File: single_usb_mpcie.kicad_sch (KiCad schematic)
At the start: 15 parts, among them J1 91304-56-052R2, J2 USB_B_Micro, U1 AZ1117H-3.3

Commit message: Change mounting holes to #6-32
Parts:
- H1, H2, H3, H4: footprint MountingHole:MountingHole_3.2mm_M3_Pad -> parts:MountingHole_6-32_Pad
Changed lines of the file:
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@@
       (effects (font (size 1.27 1.27)) (justify left))
     )
-    (property "Footprint" "MountingHole:MountingHole_3.2mm_M3_Pad" (at 124.46 147.32 0)
+    (property "Footprint" "parts:MountingHole_6-32_Pad" (at 124.46 147.32 0)
       (effects (font (size 1.27 1.27)) hide)
     )
@@
       (effects (font (size 1.27 1.27)) (justify left))
     )
-    (property "Footprint" "MountingHole:MountingHole_3.2mm_M3_Pad" (at 124.46 142.24 0)
+    (property "Footprint" "parts:MountingHole_6-32_Pad" (at 124.46 142.24 0)
       (effects (font (size 1.27 1.27)) hide)
     )
@@
       (effects (font (size 1.27 1.27)) (justify left))
     )
-    (property "Footprint" "MountingHole:MountingHole_3.2mm_M3_Pad" (at 124.46 132.08 0)
+    (property "Footprint" "parts:MountingHole_6-32_Pad" (at 124.46 132.08 0)
       (effects (font (size 1.27 1.27)) hide)
     )
@@
       (effects (font (size 1.27 1.27)) (justify left))
     )
-    (property "Footprint" "MountingHole:MountingHole_3.2mm_M3_Pad" (at 124.46 137.16 0)
-      (effects (font (size 1.27 1.27)) hide)
-    )
+    (property "Footprint" "parts:MountingHole_6-32_Pad" (at 124.46 137.16 0)
+      (effects (font (size 1.27 1.27)) hide)
+    )

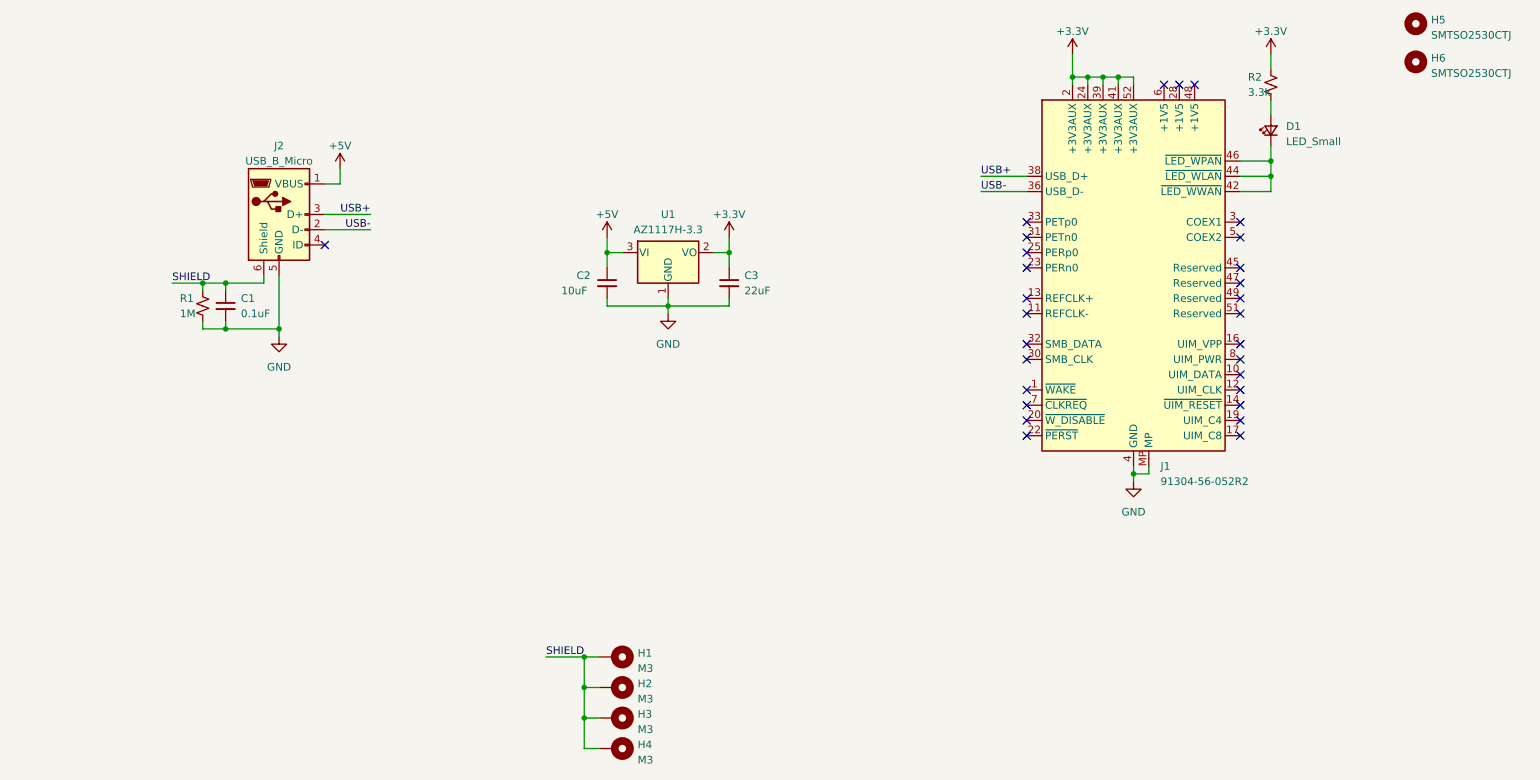
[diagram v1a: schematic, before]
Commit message: Add ESD on USB lines. Add noise filtering to VBUS. Change to a 4-layer board with ground / power planes.
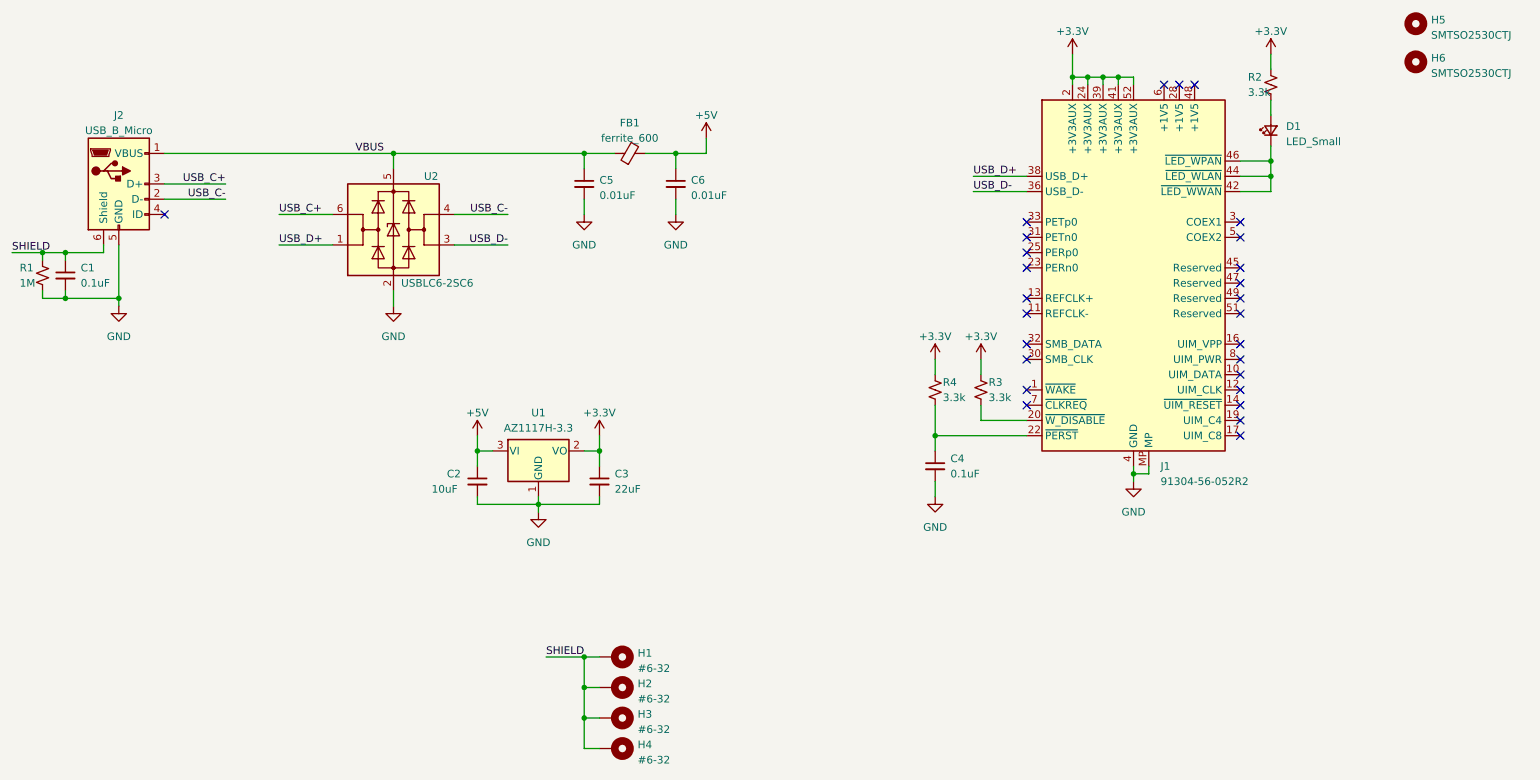
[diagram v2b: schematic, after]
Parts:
- added C4: 0.1uF, Capacitor_SMD:C_0603_1608Metric, symbol Device:C_Small
- added C5, C6: 0.01uF, Capacitor_SMD:C_0603_1608Metric, symbol Device:C_Small
- added FB1: ferrite_600, Inductor_SMD:L_0603_1608Metric, symbol Device:FerriteBead_Small
- added R3, R4: 3.3k, Resistor_SMD:R_0603_1608Metric, symbol Device:R_Small_US
- added U2: USBLC6-2SC6, Package_TO_SOT_SMD:SOT-23-6, symbol Power_Protection:USBLC6-2SC6
- C1: LCSC (none) -> C14663
- H1, H2, H3, H4: value M3 -> #6-32
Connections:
- net +3.3V: now also R3.1, R4.1
- net +5V: now also C6.1, FB1.2; no longer J2.1 (VBUS)
- net GND: now also C4.2, C5.2, C6.2, U2.2 (GND)
- net at J1.20 (~{W_DISABLE}): now also R3.2
- net at J1.22 (~{PERST}): now also C4.1, R4.2
- net USB+ renamed USB_C+
- net USB_C+: now also U2.6 (I/O1); no longer J1.38 (USB_D+)
- net USB- renamed USB_C-
- net USB_C-: now also U2.4 (I/O2); no longer J1.36 (USB_D-)
- new net USB_D+: J1.38 (USB_D+), U2.1 (I/O1)
- new net USB_D-: J1.36 (USB_D-), U2.3 (I/O2)
- new net VBUS: C5.1, FB1.1, J2.1 (VBUS), U2.5 (VBUS)
- no-connect marks 29 -> 27
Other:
- moved on the sheet: C1, C2, C3, J2, R1, U1
